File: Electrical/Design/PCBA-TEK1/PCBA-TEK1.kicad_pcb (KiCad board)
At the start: 4 copper layers, 100 x 100 mm, 177 parts, among them J501 Conn_01x04, J502 Conn_01x04, J503 Conn_01x04, J504 Conn_01x04, J505 Conn_01x04, J506 Conn_01x04, J507 Conn_01x04, J508 Conn_01x04, J601 TYPE-C-32-M-12, J701 C5137195, J702 Conn_02x05_Odd_Even, J799 Conn_01x02, SW1001 C2905169, SW1002 C2905169, SW1003 C2905169, SW1004 C2905169, SW701 C255807, SW702 C2905169, SW703 C2905169, U1001 74HC4051, U1002 74HC4051, U1003 DISPLAY_TEK1, U601 C5451661, U602 LN1134A332MR-G, U703 RP2040, U704 ESP32-S3FN8, U705 W25Q64JVSSIQ, U801 74HC165, Y701 40MHz

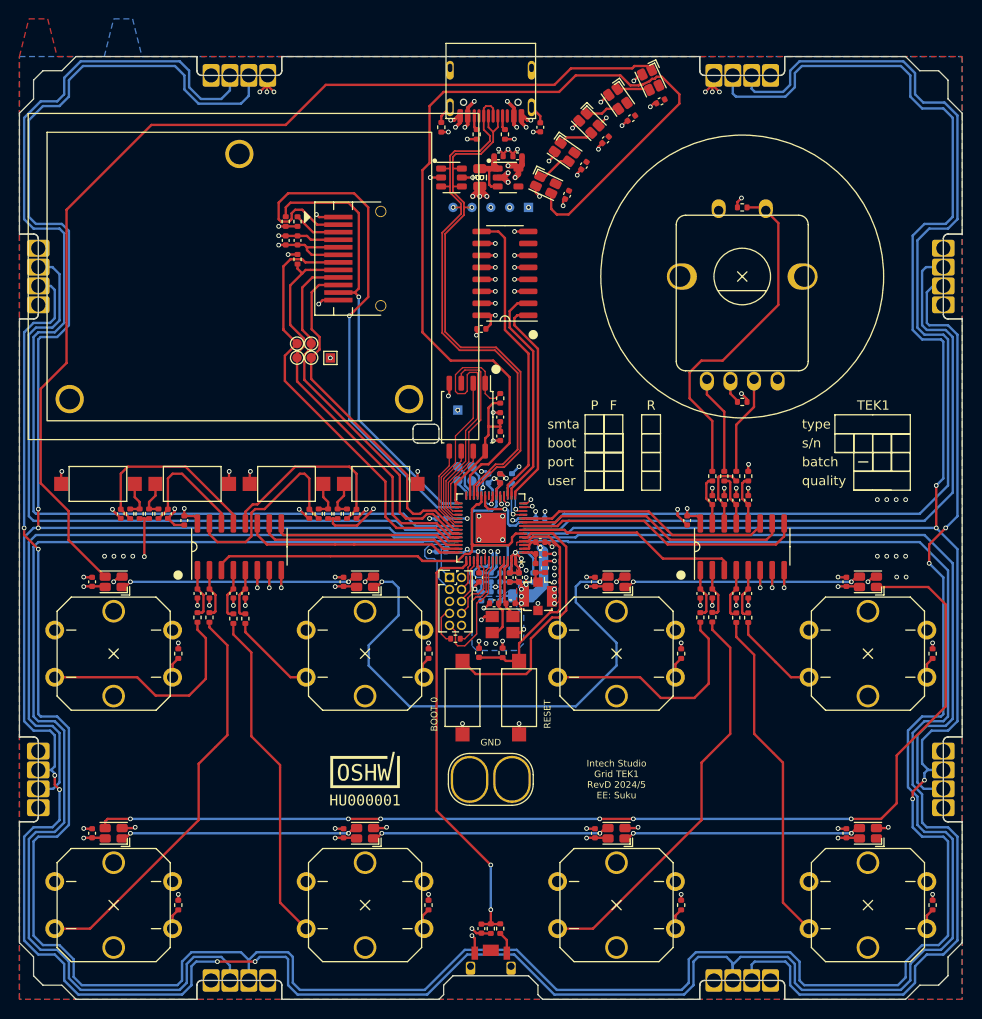
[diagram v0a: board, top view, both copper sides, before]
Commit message: SUKU TEK1 hwcfg updated for multivariant configuration
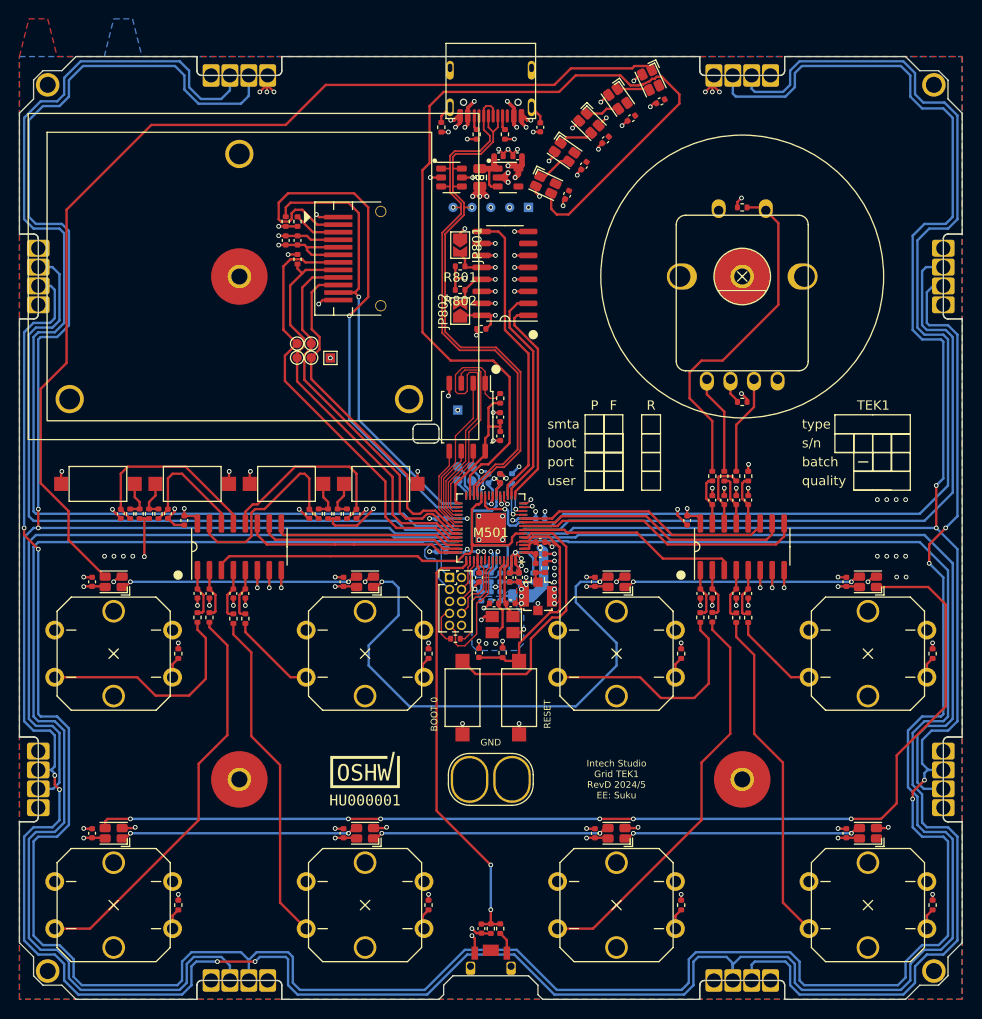
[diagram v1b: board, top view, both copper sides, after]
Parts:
- added JP801: (NF), Jumper:SolderJumper-2_P1.3mm_Open_TrianglePad1.0x1.5mm, F.Cu at (96.8, 70.0)
- added JP802: (NF), Jumper:SolderJumper-2_P1.3mm_Open_TrianglePad1.0x1.5mm, F.Cu at (96.8, 77.0)
- added M501: Conn_01x08, suku_basics:grid_outline, F.Cu at (100.0, 100.0)
- added R801: 5k1, suku_basics:RES_0402, F.Cu at (96.8, 72.2)
- added R802: 5k1, suku_basics:RES_0402, F.Cu at (96.8, 74.8)
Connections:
- U801 pad 11: +3V3 -> GND
- U801 pad 12: +3V3 -> Net-(JP801-B)
- U801 pad 13: +3V3 -> Net-(JP802-B)
- U801 pad 14: GND -> +3V3
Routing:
- net Net-(JP802-B): track 0.00 -> 5.42 mm, vias 0 -> 1
- net Net-(JP801-B): track 0.00 -> 4.76 mm, vias 0 -> 1
- net GND: track 154.1 -> 157.7 mm, vias 120 -> 121
- net +3V3: track 93.2 -> 93.9 mm, vias 41 -> 40

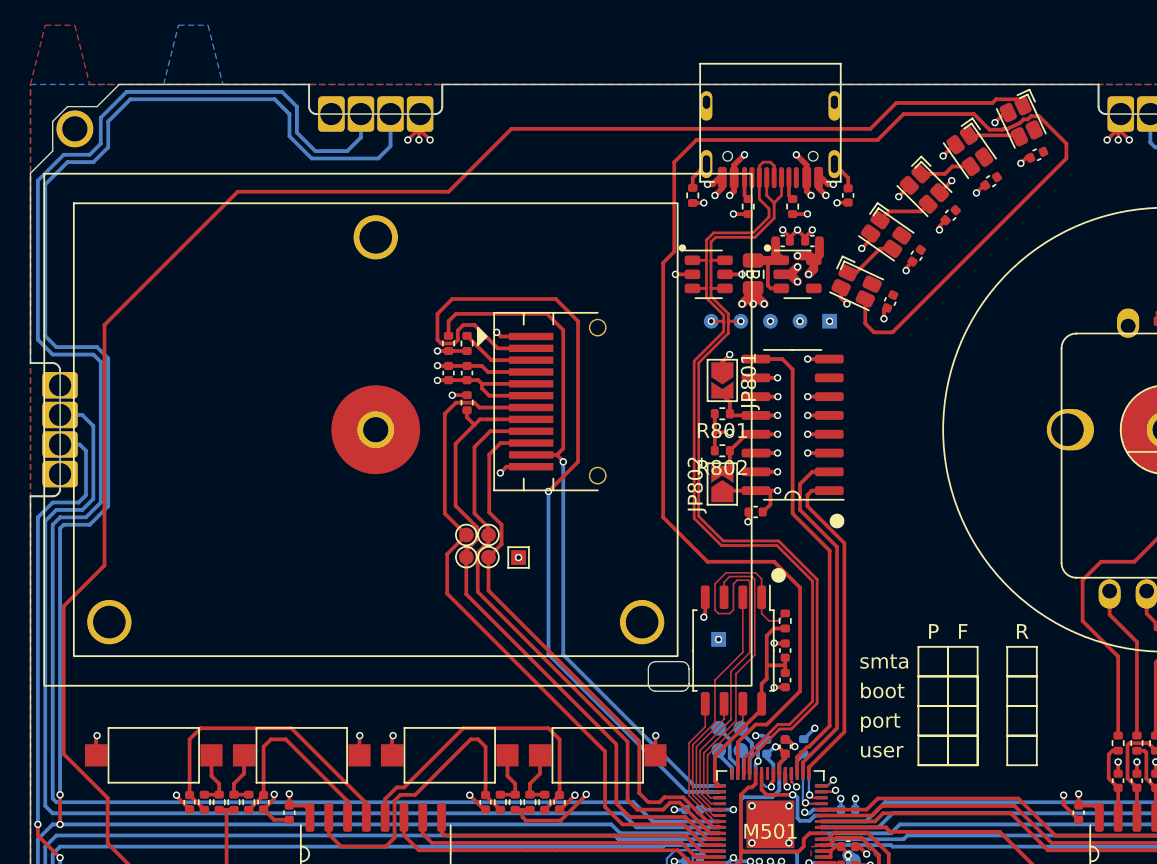
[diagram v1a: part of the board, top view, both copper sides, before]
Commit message: SUKU extra led's added for mirrored variant
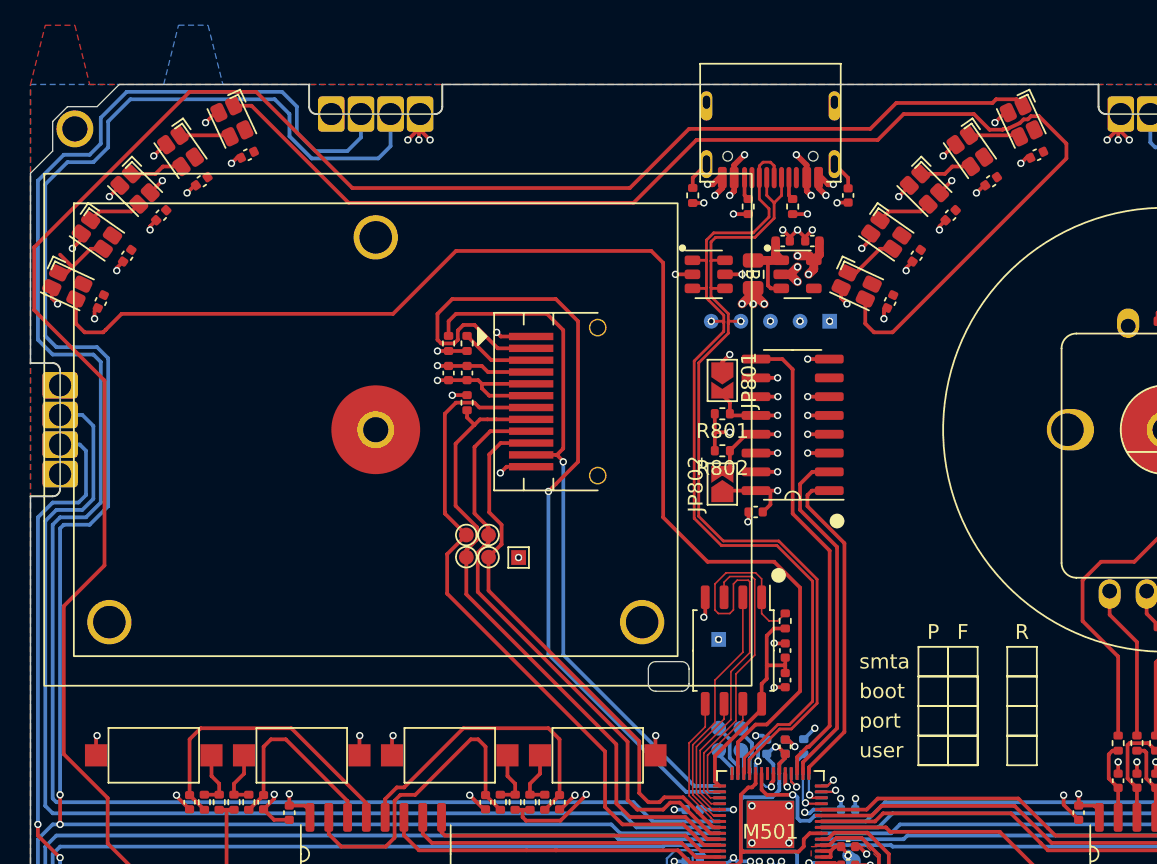
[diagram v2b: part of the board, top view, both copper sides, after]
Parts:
- added C901: 100n, suku_basics:CAP_0402, F.Cu at (54.8, 64.7)
- added C902: 100n, suku_basics:CAP_0402, F.Cu at (56.5, 61.6)
- added C903: 100n, suku_basics:CAP_0402, F.Cu at (58.8, 58.8)
- added C904: 100n, suku_basics:CAP_0402, F.Cu at (61.6, 56.5)
- added C905: 100n, suku_basics:CAP_0402, F.Cu at (64.7, 54.8)
- added D901: WS2812C-2020, suku_basics:UI_WS2812C-2020, F.Cu at (52.5, 63.6)
- added D902: WS2812C-2020, suku_basics:UI_WS2812C-2020, F.Cu at (54.5, 60.1)
- added D903: WS2812C-2020, suku_basics:UI_WS2812C-2020, F.Cu at (57.1, 57.1)
- added D904: WS2812C-2020, suku_basics:UI_WS2812C-2020, F.Cu at (60.1, 54.5)
- added D905: WS2812C-2020, suku_basics:UI_WS2812C-2020, F.Cu at (63.6, 52.5)
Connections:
- D906 pad 3: /MCU/LED_DATA_OUT -> Net-(D905-DOUT)
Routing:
- net Net-(D905-DOUT): track 0.00 -> 84.4 mm
- net Net-(D910-DOUT): track 111.5 -> 126.6 mm
- net /MCU/LED_DATA_OUT: track 101.0 -> 87.4 mm
- net GND: track 157.7 -> 167.6 mm, vias 121 -> 131
- net Net-(D901-DOUT): track 0.00 -> 4.86 mm
- net Net-(D902-DOUT): track 0.00 -> 3.69 mm
- net Net-(D903-DOUT): track 0.00 -> 3.59 mm
- net Net-(D904-DOUT): track 0.00 -> 3.46 mm
- net +5V: track 42.5 -> 43.7 mm, vias 38 -> 39

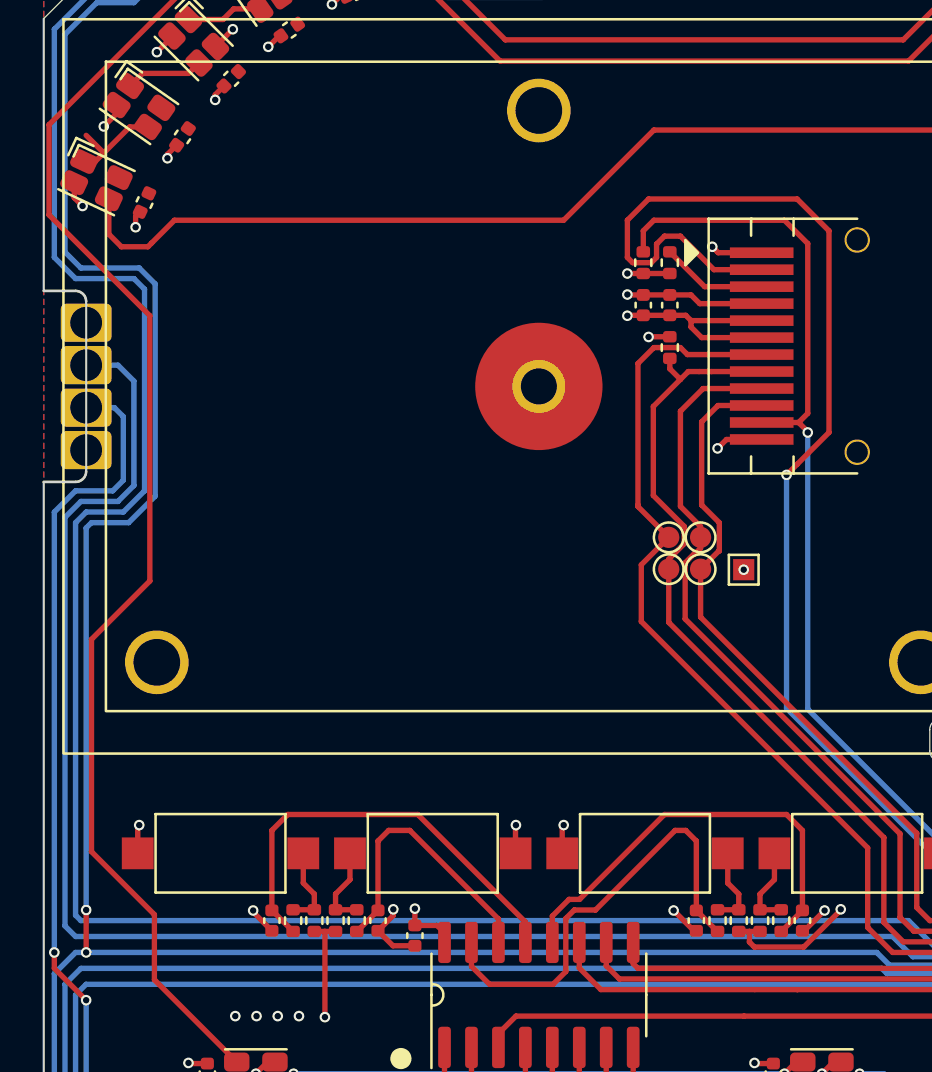
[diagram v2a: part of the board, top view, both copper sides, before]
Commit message: SUKU reverse endless pot progress but not routed yet
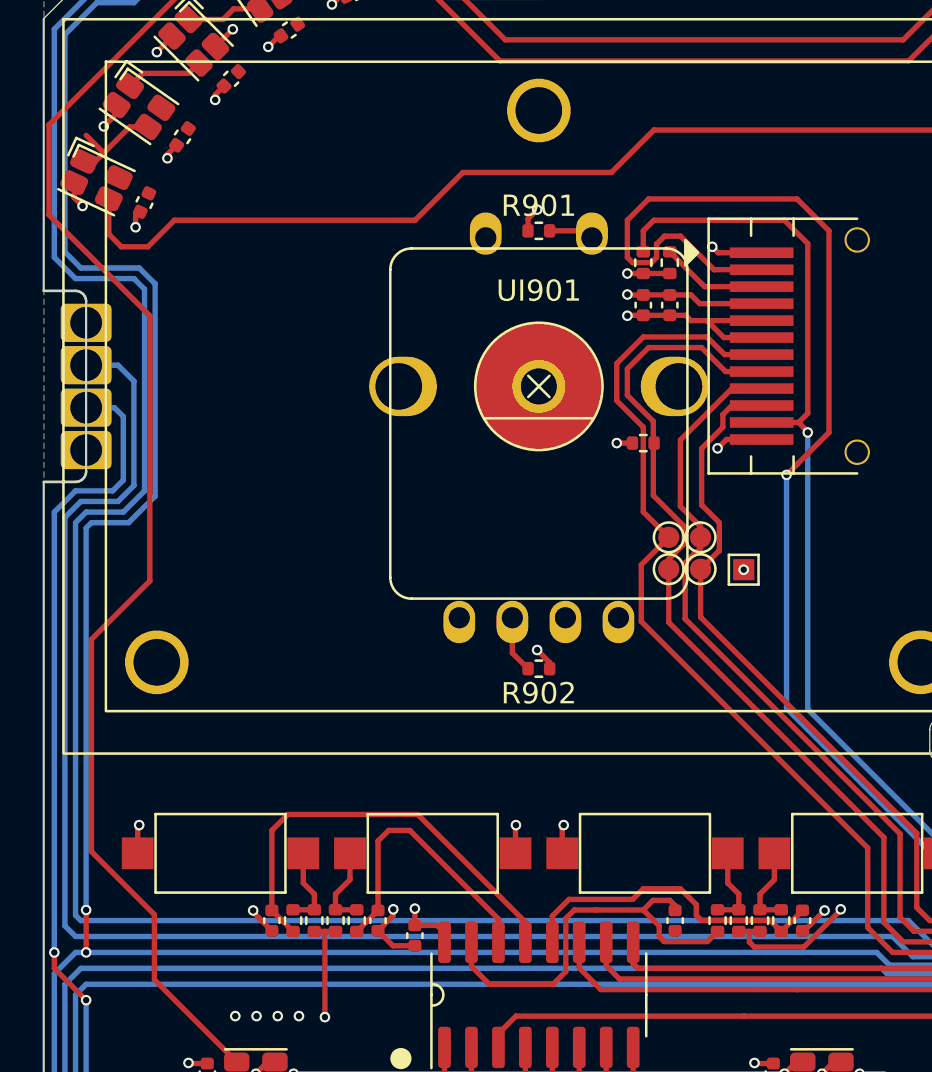
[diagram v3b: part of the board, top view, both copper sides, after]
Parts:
- added R901: 5k1, suku_basics:RES_0402, F.Cu at (73.3, 66.0)
- added R902: 470R, suku_basics:RES_0402, F.Cu at (73.3, 86.6)
- added UI901: P090S-04F20BR10K (NF), suku_basics:UI_ENDLESSPOTSW_ALPHA, F.Cu at (73.3, 73.3)
- moved R1018 4.67 mm to (78.2, 76.0), turned to 180 degrees
- moved C1002 1.00 mm to (79.8, 98.5)
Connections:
- R1014 pad 2: GND -> /ANA_7
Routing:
- net Net-(U1001-X3): track 20.5 -> 15.1 mm
- net GND: track 167.6 -> 164.5 mm, vias 131 -> 129
- net Net-(R902-Pad2): track 0.00 -> 2.71 mm
- net ESP_GPIO_33: track 44.4 -> 46.9 mm
- net Net-(U1001-X2): track 21.4 -> 19.1 mm
- net /ANA_4: track 3.88 -> 6.00 mm
- net +3V3: track 93.9 -> 95.9 mm, vias 40 -> 42
- net ESP_GPIO_34: track 47.2 -> 49.0 mm
- net ESP_GPIO_47: track 40.6 -> 39.8 mm
- net /ANA_7: track 0.00 -> 0.76 mm, vias 0 -> 1

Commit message: SUKU symetrical mini button layout done
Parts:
- removed R703: 5k1, suku_basics:RES_0402
- added JP901: (NF), Jumper:SolderJumper-2_P1.3mm_Open_TrianglePad1.0x1.5mm, F.Cu at (64.8, 101.5)
- added JP902: (NF), Jumper:SolderJumper-2_P1.3mm_Open_TrianglePad1.0x1.5mm, F.Cu at (61.8, 101.5)
- added JP903: (NF), Jumper:SolderJumper-2_P1.3mm_Open_TrianglePad1.0x1.5mm, F.Cu at (115.0, 101.5)
- added JP904: (NF), Jumper:SolderJumper-2_P1.3mm_Open_TrianglePad1.0x1.5mm, F.Cu at (118.0, 101.5)
- added R907: 5k1, suku_basics:RES_0402, F.Cu at (117.0, 98.5)
- added R908: 5k1, suku_basics:RES_0402, F.Cu at (136.0, 98.5)
- added R909: 5k1, suku_basics:RES_0402, F.Cu at (137.0, 98.5)
- added SW905: C2905169, Button_Switch_SMD:SW_SPST_CK_RS282G05A3, F.Cu at (111.7, 95.3)
- added SW906: C2905169, Button_Switch_SMD:SW_SPST_CK_RS282G05A3, F.Cu at (121.7, 95.3)
- added SW907: C2905169, Button_Switch_SMD:SW_SPST_CK_RS282G05A3, F.Cu at (131.7, 95.3)
- added SW908: C2905169, Button_Switch_SMD:SW_SPST_CK_RS282G05A3, F.Cu at (141.7, 95.3)
- moved R901 53.6 mm to (116.0, 98.5), turned to -90 degrees
- moved R1010 12.2 mm to (135.0, 98.5)
- moved C1010 12.1 mm to (114.0, 98.5), turned to -90 degrees
- moved C1015 11.8 mm to (139.0, 98.5), turned to -90 degrees
- moved R1014 11.4 mm to (138.0, 98.5)
- moved C1011 10.6 mm to (134.0, 98.5)
- moved R1009 10.5 mm to (115.0, 98.5)
- moved R1013 8.97 mm to (118.0, 98.5)
- moved C1014 5.95 mm to (119.0, 98.5), turned to -90 degrees
- moved C1002 1.00 mm to (80.8, 98.5), turned to 90 degrees
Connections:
- R1021 pad 2: +3V3 -> Net-(JP902-B)
- R1022 pad 2: +3V3 -> Net-(JP901-B)
- R901 pad 1: +3V3 -> /ANA_2
- R901 pad 2: /ANA_4 -> Net-(JP903-B)
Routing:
- net Net-(U1002-X0): track 5.33 -> 50.9 mm
- net /ANA_4: track 6.00 -> 47.2 mm
- net Net-(U1001-X0): track 20.5 -> 50.9 mm
- net /ANA_1: track 3.94 -> 21.6 mm
- net /ANA_0: track 3.88 -> 18.0 mm
- net Net-(U1002-X2): track 5.26 -> 17.2 mm
- net /ANA_3: track 10.5 -> 21.6 mm
- net /ANA_6: track 36.6 -> 47.2 mm
- net Net-(U1002-X3): track 5.26 -> 14.8 mm
- net GND: track 164.5 -> 173.4 mm, vias 129 -> 133
- net /ANA_2: track 10.5 -> 18.0 mm
- net +3V3: track 95.9 -> 102.4 mm
- net Net-(U1002-X1): track 7.32 -> 13.4 mm
- net /ANA_7: track 0.76 -> 3.94 mm, vias 1 -> 0
- net Net-(JP904-B): track 0.00 -> 2.32 mm
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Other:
- board text added: "L-SCR"
- board text added: "R-SCR"
- board text removed: "F"
- board text removed: "P"
- board text removed: "R"
- board text removed: "TEK1"
- board text removed: "batch"
- board text removed: "boot"
- board text removed: "port"
- board text removed: "quality"
- board text removed: "s/n"
- board text removed: "smta"
- board text removed: "type"
- board text removed: "user"
